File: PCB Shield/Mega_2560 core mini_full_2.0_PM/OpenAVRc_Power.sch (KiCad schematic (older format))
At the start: 18 parts, among them P17 BATT, P21 Sw_power, P26 LCD_Alim, P29 Sw_On, P30 MiniDCDC3A, U4 PM5033, U5 LD1117S33TR

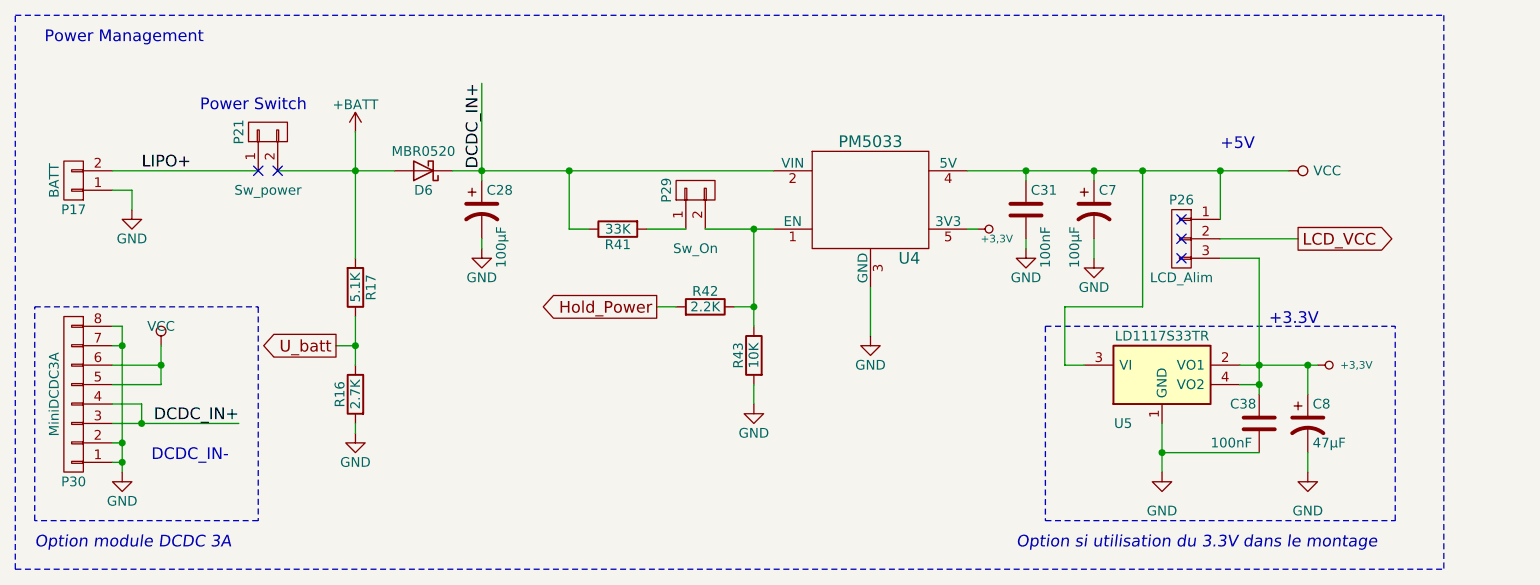
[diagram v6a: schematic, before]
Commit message: Re-update_shield_schéma
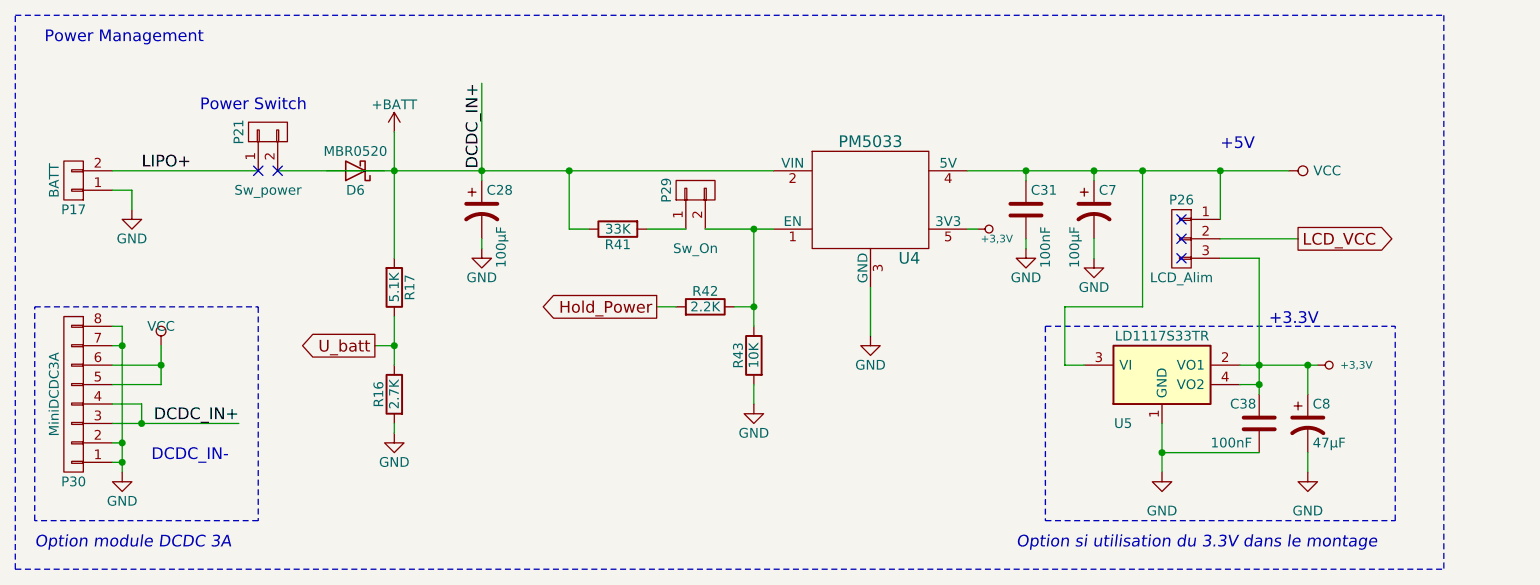
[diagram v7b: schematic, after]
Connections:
- net +BATT: now also C28.1, P30.3 (P3), P30.4 (P4), R41.1, U4.2 (VIN); no longer D6.2 (A)
- removed net DCDC_IN+: C28.1, D6.1 (K), P30.3 (P3), P30.4 (P4), R41.1, U4.2 (VIN)
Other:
- moved on the sheet: D6, R16, R17
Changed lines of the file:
@@
 Sheet 7 7
 Title "Shield Mega2560 core Full"
-Date "2017-11-12"
+Date "2018-01-27"
 Rev "2.00"
 Comp "© Team OpenAVRc"
@@
 L R-RESCUE-Mega_2560_core_mini_full_2.0 R16
 U 1 1 59C53138
-P 4050 4150
-F 0 "R16" V 4130 4150 50  0000 C CNN
-F 1 "2.7K" V 4050 4150 50  0000 C CNN
-F 2 "Resistors_SMD:R_1206" V 3980 4150 50  0001 C CNN
-F 3 "" H 4050 4150 50  0000 C CNN
-	1    4050 4150
+P 4250 4150
+F 0 "R16" V 4330 4150 50  0000 C CNN
+F 1 "2.7K" V 4250 4150 50  0000 C CNN
+F 2 "Resistors_SMD:R_1206" V 4180 4150 50  0001 C CNN
+F 3 "" H 4250 4150 50  0000 C CNN
+	1    4250 4150
 	-1   0    0    -1
 $EndComp
@@
 L GND-RESCUE-Mega_2560_core_mini_full_2.0 #PWR0116
 U 1 1 59C53163
-P 4050 4350
-F 0 "#PWR0116" H 4050 4100 50  0001 C CNN
-F 1 "GND" H 4050 4200 50  0000 C CNN
-F 2 "" H 4050 4350 50  0000 C CNN
-F 3 "" H 4050 4350 50  0000 C CNN
-	1    4050 4350
+P 4250 4350
+F 0 "#PWR0116" H 4250 4100 50  0001 C CNN
+F 1 "GND" H 4250 4200 50  0000 C CNN
+F 2 "" H 4250 4350 50  0000 C CNN
+F 3 "" H 4250 4350 50  0000 C CNN
+	1    4250 4350
 	1    0    0    -1
 $EndComp
@@
 L R-RESCUE-Mega_2560_core_mini_full_2.0 R17
 U 1 1 59C53182
-P 4050 3600
-F 0 "R17" V 4130 3600 50  0000 C CNN
-F 1 "5.1K" V 4050 3600 50  0000 C CNN
-F 2 "Resistors_SMD:R_1206" V 3980 3600 50  0001 C CNN
-F 3 "" H 4050 3600 50  0000 C CNN
-	1    4050 3600
+P 4250 3600
+F 0 "R17" V 4330 3600 50  0000 C CNN
+F 1 "5.1K" V 4250 3600 50  0000 C CNN
+F 2 "Resistors_SMD:R_1206" V 4180 3600 50  0001 C CNN
+F 3 "" H 4250 3600 50  0000 C CNN
+	1    4250 3600
 	1    0    0    1
 $EndComp
@@
 L MBR0520 D6
 U 1 1 59C5319C
-P 4400 3000
-F 0 "D6" H 4400 3100 50  0000 C CNN
-F 1 "MBR0520" H 4400 2900 50  0000 C CNN
-F 2 "Diodes_SMD:D_SOD-123" H 4400 2825 50  0001 C CNN
-F 3 "" H 4400 3000 50  0001 C CNN
-	1    4400 3000
+P 4050 3000
+F 0 "D6" H 4050 3100 50  0000 C CNN
+F 1 "MBR0520" H 4050 2900 50  0000 C CNN
+F 2 "Diodes_SMD:D_SOD-123" H 4050 2825 50  0001 C CNN
+F 3 "" H 4050 3000 50  0001 C CNN
+	1    4050 3000
 	-1   0    0    1
 $EndComp
@@
 L +BATT #PWR0126
 U 1 1 59C53200
-P 4050 2800
-F 0 "#PWR0126" H 4050 2650 50  0001 C CNN
-F 1 "+BATT" H 4050 2940 50  0000 C CNN
-F 2 "" H 4050 2800 50  0000 C CNN
-F 3 "" H 4050 2800 50  0000 C CNN
-	1    4050 2800
+P 4250 2800
+F 0 "#PWR0126" H 4250 2650 50  0001 C CNN
+F 1 "+BATT" H 4250 2940 50  0000 C CNN
+F 2 "" H 4250 2800 50  0000 C CNN
+F 3 "" H 4250 2800 50  0000 C CNN
+	1    4250 2800
 	1    0    0    -1
 $EndComp
 Text Label 4700 2550 3    60   ~ 0
 DCDC_IN+
-Text GLabel 3950 3900 0    60   Output ~ 0
+Text GLabel 4150 3900 0    60   Output ~ 0
 U_batt
 Text GLabel 8900 3350 2    60   Output ~ 0
@@
 	7600 3800 9400 3800
 Wire Wire Line
-	7200 3000 8850 3000
+	7200 3000 7500 3000
+Wire Wire Line
+	7500 3000 7850 3000
+Wire Wire Line
+	7850 3000 8100 3000
+Wire Wire Line
+	8100 3000 8500 3000
+Wire Wire Line
+	8500 3000 8850 3000
 Wire Notes Line
 	7600 4800 9400 4800
@@
 	8500 3350 8900 3350
 Wire Wire Line
-	8200 4300 8200 4550
+	8200 4300 8200 4450
+Wire Wire Line
+	8200 4450 8200 4550
 Wire Wire Line
 	6700 3600 6700 3850
 Wire Wire Line
-	4700 2550 4700 3050
+	4700 2550 4700 3000
+Wire Wire Line
+	4700 3000 4700 3050
 Connection ~ 4700 3000
 Wire Wire Line
@@
 	8950 4550 8950 4450
 Wire Wire Line
-	2800 4300 3450 4300
+	2800 4300 2950 4300
+Wire Wire Line
+	2950 4300 3450 4300
 Wire Wire Line
 	2800 4200 2950 4200
@@
 	2850 4400 2800 4400
 Wire Wire Line
-	2850 3800 2850 4550
+	2850 3800 2850 3900
+Wire Wire Line
+	2850 3900 2850 4400
+Wire Wire Line
+	2850 4400 2850 4500
+Wire Wire Line
+	2850 4500 2850 4550
 Wire Wire Line
 	2800 3900 2850 3900
@@
 	3050 4100 2800 4100
 Wire Wire Line
-	3050 3900 3050 4100
+	3050 3900 3050 4000
+Wire Wire Line
+	3050 4000 3050 4100
 Wire Wire Line
 	3050 4000 2800 4000
@@
 	2300 2200 9650 2200
 Wire Wire Line
-	4050 3750 4050 4000
-Connection ~ 4050 3900
-Wire Wire Line
-	4050 4350 4050 4300
-Wire Wire Line
-	4050 2800 4050 3450
-Connection ~ 4050 3000
-Wire Wire Line
-	4550 3000 6200 3000
+	4250 3750 4250 3900
+Wire Wire Line
+	4250 3900 4250 4000
+Connection ~ 4250 3900
+Wire Wire Line
+	4250 4350 4250 4300
+Wire Wire Line
+	4250 2800 4250 3000
+Wire Wire Line
+	4250 3000 4250 3450
+Connection ~ 4250 3000
 Wire Wire Line
 	3650 3000 4250 3000
+Wire Wire Line
+	4250 3000 4700 3000
+Wire Wire Line
+	4700 3000 5150 3000
+Wire Wire Line
+	5150 3000 6200 3000
 Wire Notes Line
 	9400 4800 9400 3800
 Wire Wire Line
-	8600 4000 9000 4000
+	8600 4000 8700 4000
+Wire Wire Line
+	8700 4000 8950 4000
+Wire Wire Line
+	8950 4000 9000 4000
 Connection ~ 8700 4000
 Wire Wire Line
@@
 	9650 2200 9650 5050
 Wire Wire Line
-	8700 3450 8700 4150
+	8700 3450 8700 4000
+Wire Wire Line
+	8700 4000 8700 4100
+Wire Wire Line
+	8700 4100 8700 4150
 Wire Wire Line
 	8700 3450 8500 3450
@@
 	6000 3700 6100 3700
 Wire Wire Line
-	6100 3300 6100 3800
-Wire Wire Line
-	5850 3300 6200 3300
+	6100 3300 6100 3700
+Wire Wire Line
+	6100 3700 6100 3800
+Wire Wire Line
+	5850 3300 6100 3300
+Wire Wire Line
+	6100 3300 6200 3300
 Connection ~ 6100 3700
 Connection ~ 6100 3300
@@
 	7700 3700 7700 4000
 Wire Wire Line
-	4050 3900 3950 3900
+	4250 3900 4150 3900
 $EndSCHEMATC
